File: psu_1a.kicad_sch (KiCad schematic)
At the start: 2 parts

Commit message: Final schematic before review.
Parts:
- renumbered R6 to R1, R7 to R2
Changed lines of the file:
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@@
 		(on_board yes)
 		(dnp no)
-		(property "Reference" "R7"
+		(property "Reference" "R2"
 			(at 62.23 62.23 90)
 			(effects
@@
 			(project ""
 				(path "/64404f27-cfd6-41d9-8edb-810ebab8cc14/304cb132-240f-469f-b7d9-31219ff2c2ac"
-					(reference "R7")
+					(reference "R2")
 					(unit 1)
 				)
@@
 		(on_board yes)
 		(dnp no)
-		(property "Reference" "R6"
+		(property "Reference" "R1"
 			(at 62.23 58.42 90)
 			(effects
@@
 			(project ""
 				(path "/64404f27-cfd6-41d9-8edb-810ebab8cc14/304cb132-240f-469f-b7d9-31219ff2c2ac"
-					(reference "R6")
+					(reference "R1")
 					(unit 1)
 				)

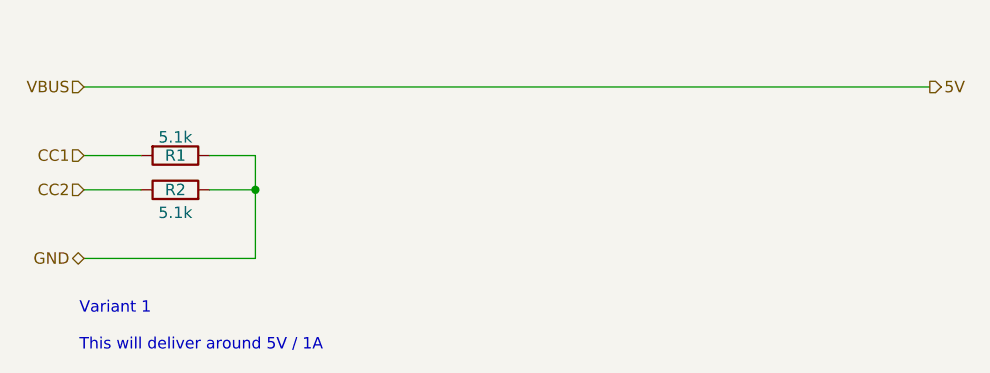
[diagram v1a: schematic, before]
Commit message: Added TVS (SMAJ5.0A) to VBUS-GND Added polyfuses to both PSUs
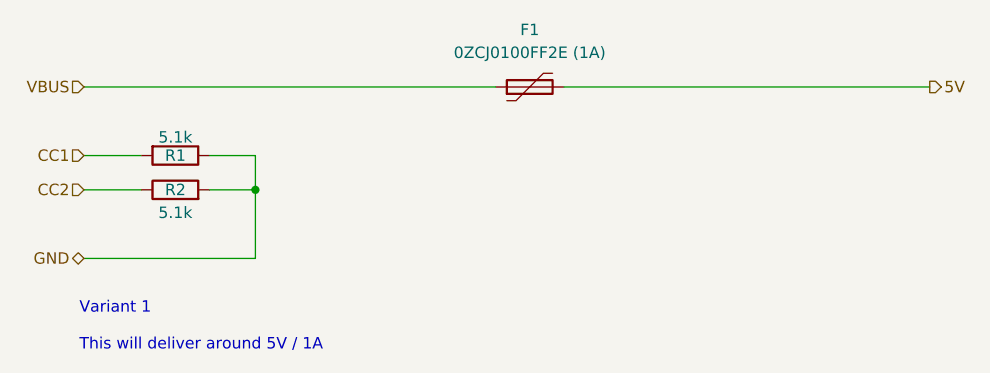
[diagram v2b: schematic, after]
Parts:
- added F1: 0ZCJ0100FF2E (1A), symbol Device:Polyfuse
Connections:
- net 5V: now also F1.2
- new net VBUS: F1.1
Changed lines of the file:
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@@
 	(wire
 		(pts
-			(xy 52.07 50.8) (xy 146.05 50.8)
+			(xy 71.12 58.42) (xy 71.12 62.23)
 		)
 		(stroke
@@
 	(wire
 		(pts
-			(xy 71.12 58.42) (xy 71.12 62.23)
+			(xy 105.41 50.8) (xy 146.05 50.8)
 		)
 		(stroke
@@
 		(pts
 			(xy 71.12 62.23) (xy 66.04 62.23)
+		)
+		(stroke
+			(width 0)
+			(type default)
+		)
+	)
+	(wire
+		(pts
+			(xy 52.07 50.8) (xy 97.79 50.8)
 		)
 		(stroke
@@
 		)
 	)
+	(symbol
+		(lib_id "Device:Polyfuse")
+		(at 101.6 50.8 90)
+		(unit 1)
+		(exclude_from_sim no)
+		(in_bom yes)
+		(on_board yes)
+		(dnp no)
+		(fields_autoplaced yes)
+		(property "Reference" "F1"
+			(at 101.6 44.45 90)
+			(effects
+				(font
+					(size 1.27 1.27)
+				)
+			)
+		)
+		(property "Value" "0ZCJ0100FF2E (1A)"
+			(at 101.6 46.99 90)
+			(effects
+				(font
+					(size 1.27 1.27)
+				)
+			)
+		)
+		(property "Footprint" ""
+			(at 106.68 49.53 0)
+			(effects
+				(font
+					(size 1.27 1.27)
+				)
+				(justify left)
+				(hide yes)
+			)
+		)
+		(property "Datasheet" "~"
+			(at 101.6 50.8 0)
+			(effects
+				(font
+					(size 1.27 1.27)
+				)
+				(hide yes)
+			)
+		)
+		(property "Description" "Resettable fuse, polymeric positive temperature coefficient"
+			(at 101.6 50.8 0)
+			(effects
+				(font
+					(size 1.27 1.27)
+				)
+				(hide yes)
+			)
+		)
+		(pin "2"
+		)
+		(pin "1"
+		)
+		(instances
+			(project ""
+				(path "/64404f27-cfd6-41d9-8edb-810ebab8cc14/304cb132-240f-469f-b7d9-31219ff2c2ac"
+					(reference "F1")
+					(unit 1)
+				)
+			)
+		)
+	)

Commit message: Re-labelled all parts.
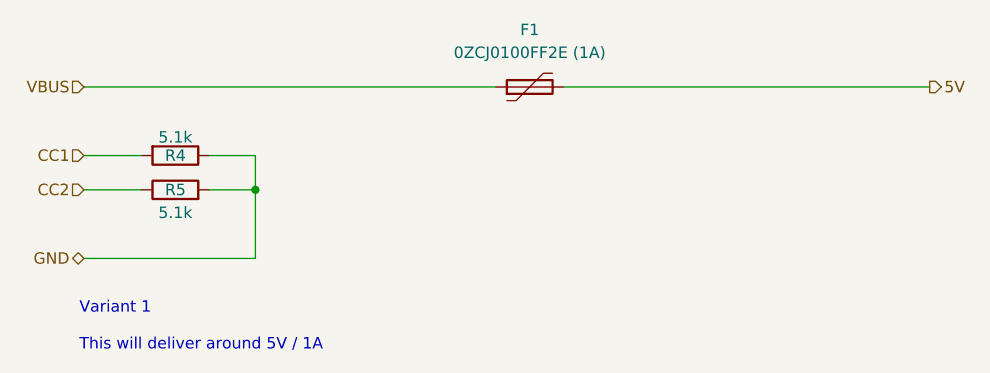
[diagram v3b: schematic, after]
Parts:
- renumbered R1 to R4, R2 to R5
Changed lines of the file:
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@@
 		(on_board yes)
 		(dnp no)
-		(property "Reference" "R2"
+		(property "Reference" "R5"
 			(at 62.23 62.23 90)
 			(effects
@@
 			(project ""
 				(path "/64404f27-cfd6-41d9-8edb-810ebab8cc14/304cb132-240f-469f-b7d9-31219ff2c2ac"
-					(reference "R2")
+					(reference "R5")
 					(unit 1)
 				)
@@
 		(on_board yes)
 		(dnp no)
-		(property "Reference" "R1"
+		(property "Reference" "R4"
 			(at 62.23 58.42 90)
 			(effects
@@
 			(project ""
 				(path "/64404f27-cfd6-41d9-8edb-810ebab8cc14/304cb132-240f-469f-b7d9-31219ff2c2ac"
-					(reference "R1")
+					(reference "R4")
 					(unit 1)
 				)

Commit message: Reorganized board to be on one sheet.
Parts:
- removed F1: 0ZCJ0100FF2E (1A), symbol Device:Polyfuse
- removed R4, R5: 5.1k, symbol Device:R
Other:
- note removed: "Variant 1 This will deliver around 5V / 1A"
